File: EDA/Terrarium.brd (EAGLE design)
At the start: 109.2 x 63.2 mm, 20 parts, among them J1 LEDSTRIP, J3 OLED, J4 DHT22, J5 PWR, J7 WATER, Q1 2N3904, Q2 2N3904

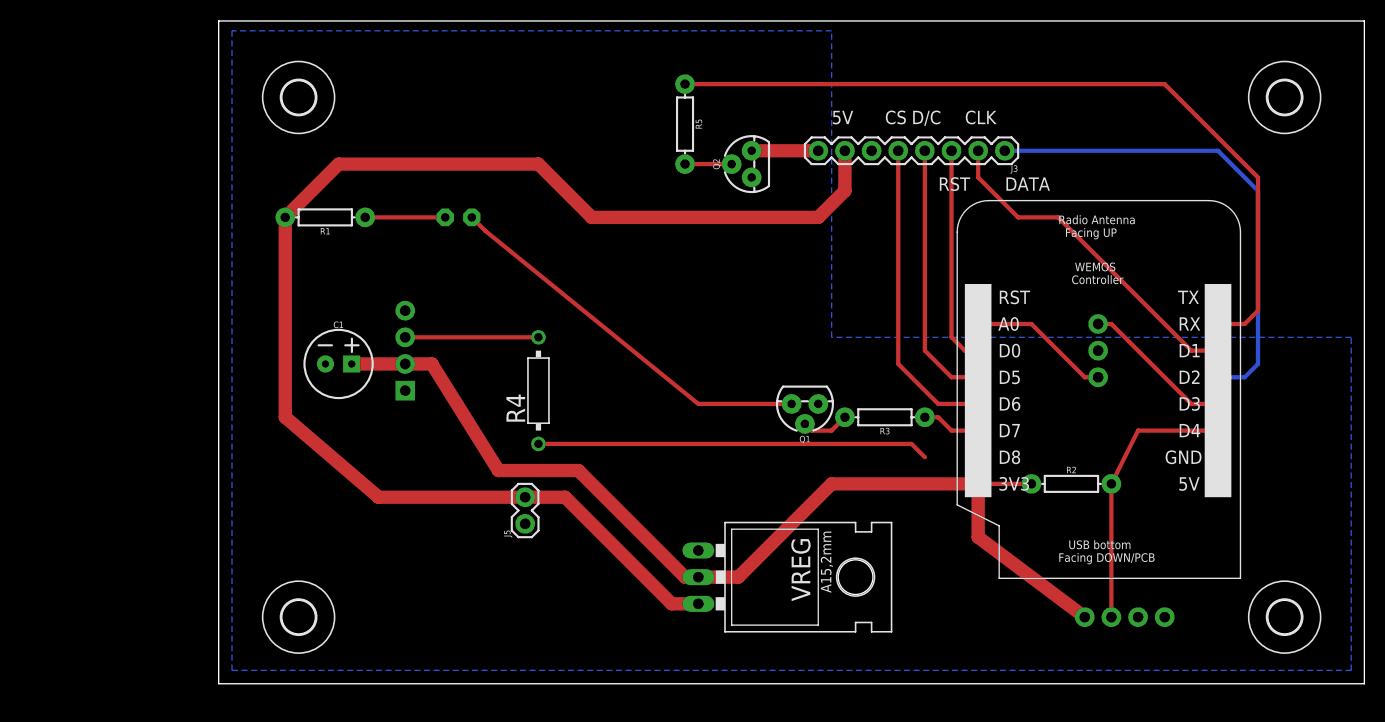
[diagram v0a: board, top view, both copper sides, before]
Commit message: Continuing improvements
1. Update Eagle files for new layout
2. Update text placement on OLED
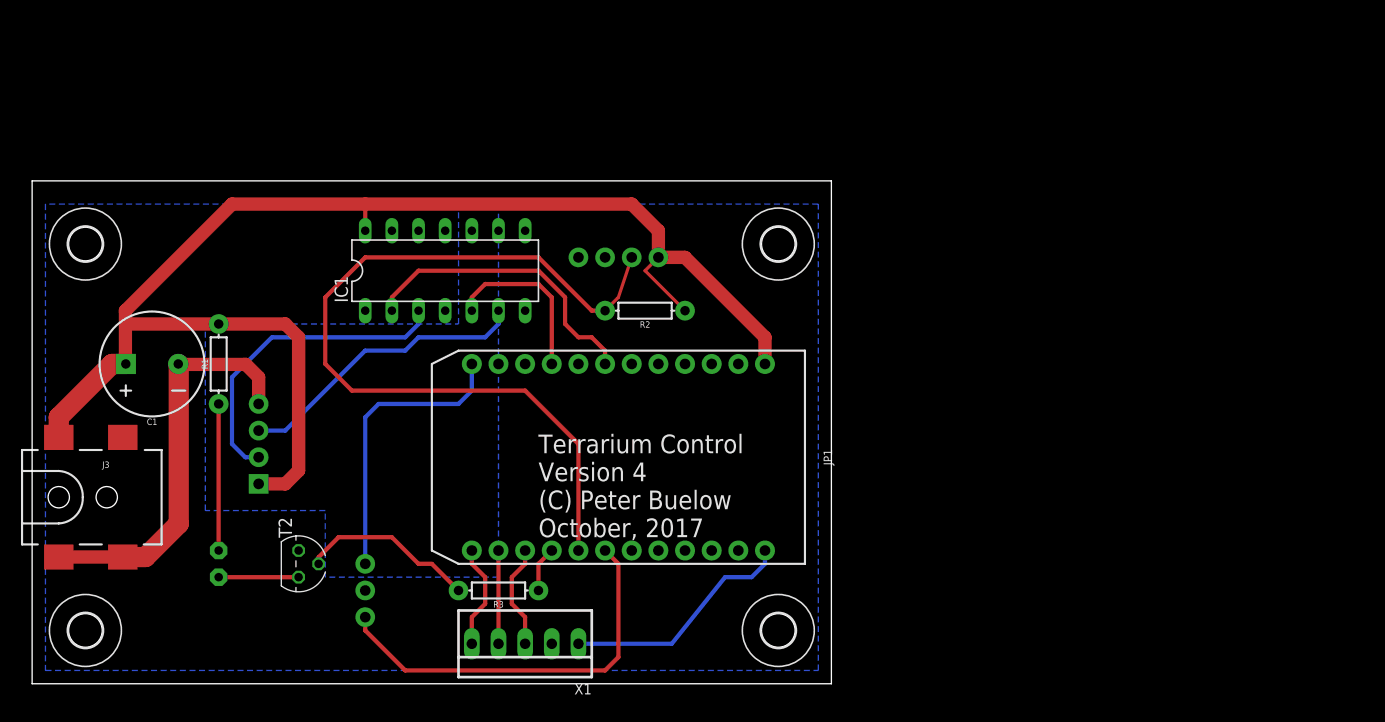
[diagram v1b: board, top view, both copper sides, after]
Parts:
- removed J5: PWR, SparkFun-Connectors:1X02
- removed LED10: UV, adafruit:LED5MM
- removed Q1, Q2: 2N3904, SparkFun-DiscreteSemi:TO-92
- removed R4: 470ohm, resistor-power:RS1/4
- removed R5: 1k, SparkFun-Resistors:AXIAL-0.3
- removed U$1: WEMOS, wemos:WEMOS
- removed VREG: LD1117VXX, SparkFun-IC-Power:78XXL
- added IC1: 74LS125N, adafruit:DIL14
- added JP1: PARTICLE_PHOTON, SparkFun-Boards:PARTICLE_PHOTON
- added LED: UV, adafruit:LED5MM
- added T2: 2N3904, transistor:TO92
- added X1: 22-23-2051, con-molex:22-23-2051
- C1: value 100uF -> 1mf; device SparkFun-Capacitors:CPOL-RADIAL-2.5MM-6.5MM -> SparkFun-Capacitors:CPOL-RADIAL-5MM-10MM-KIT
- J3: value OLED -> 5.5x2.1mm Barrel; device SparkFun-Connectors:1X08 -> SparkFun-Connectors:POWER_JACK_SMD
- R1: value 100 -> 65
- R2: value 10k -> 4.7k
- R3: value 1k -> 10k
- moved J3 96.0 mm to (2.54, 17.8), turned to 0 degrees
- moved J7 72.1 mm to (31.8, 11.4), turned to 270 degrees
- moved J4 53.2 mm to (59.7, 40.6), turned to 0 degrees
- moved H4 50.2 mm to (71.1, 41.9)
- moved H3 48.3 mm to (71.1, 5.08)
- moved R2 43.9 mm to (58.4, 35.6), turned to 180 degrees
- moved R3 40.4 mm to (44.5, 8.89)
- moved H1 24.7 mm to (5.08, 41.9)
- moved H2 20.4 mm to (5.08, 5.08)
- moved C1 17.8 mm to (11.4, 30.5), turned to 180 degrees
- moved R1 17.3 mm to (17.8, 30.5), turned to 90 degrees
- moved J1 16.6 mm to (21.6, 19.1)
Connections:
- removed net 3V3: C1.1, J1.2, J4.1, R2.P$1, U$1.3V3, VREG.GND
- removed net 5V: J3.7, J5.2, R1.P$2, VREG.OUT
- removed net CS: J3.5, U$1.D6
- removed net DC: J3.4, U$1.D5
- removed net DINLIGHT: J1.3, R4.2
- removed net LED_DIN: R4.1, U$1.D8
- removed net N$1: J3.8, Q2.3
- removed net OLEDPW: R5.P$1, U$1.RX
- removed net RST: J3.3, U$1.D0
- removed net SCL: J3.2, U$1.D1
- removed net SDA: J3.1, U$1.D2
- removed net UVPWR: R3.P$1, U$1.D7
- new net +3V3: JP1.24, X1.1
- new net MOSI: IC1.6, J1.3
- new net MOSI_LV: IC1.2, JP1.7
- new net N$3: JP1.13, X1.5
- new net N$7: JP1.15, X1.3
- new net SCK: IC1.3, J1.2
- new net SCK_LV: IC1.5, JP1.9
- new net UV: JP1.16, R3.P$1
- new net VBAT: JP1.22
- new net VIN: C1.+, IC1.14, J1.1, J3.VIN0, J4.1, JP1.1, R1.P$2, R2.P$1
- net A0: now also JP1.12; no longer U$1.A0
- net DHT22: now also JP1.17; no longer U$1.D4
- net GND: now also C1.-, IC1.1, IC1.4, IC1.7, J3.GND, J3.P$4, JP1.2, JP1.21, T2.3, X1.2; no longer C1.2, J1.1, J5.1, Q1.1, Q2.1, U$1.GND, VREG.IN
- net MD: now also JP1.18; no longer U$1.D3
- net N$2: now also T2.2; no longer Q1.2
- net N$4: now also LED.K, T2.1; no longer LED10.K, Q1.3
- net N$5: now also LED.A; no longer LED10.A
- net N$6: now also JP1.14, X1.4; no longer Q2.2, R5.P$2
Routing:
- net VIN: track 0.00 -> 133.8 mm
- net 5V: track 127.9 -> 0.00 mm
- net 3V3: track 96.1 -> 0.00 mm
- net OLEDPW: track 75.3 -> 0.00 mm
- net DHT22: track 26.0 -> 80.0 mm
- net SDA: track 46.6 -> 0.00 mm
- net GND: track 0.00 -> 38.7 mm
- net LED_DIN: track 37.4 -> 0.00 mm
- net SCL: track 32.2 -> 0.00 mm
- net SCK: track 0.00 -> 30.6 mm
- net CS: track 29.5 -> 0.00 mm
- net N$4: track 36.9 -> 7.62 mm
- net MOSI_LV: track 0.00 -> 28.6 mm
- net MOSI: track 0.00 -> 28.3 mm
- net DC: track 25.2 -> 0.00 mm
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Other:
- board size 109.2 x 63.2 mm -> 76.2 x 47.9 mm
- board text added: "Terrarium Control Version 4 (C) Peter Buelow October, 2017"
- board text removed: "+"
- board text removed: "-"
- board text removed: "5V"
- board text removed: "A0"
- board text removed: "CLK"
- board text removed: "CS"
- board text removed: "D"
- board text removed: "D/C"
- board text removed: "D3"
- board text removed: "DATA"
- board text removed: "RST"
